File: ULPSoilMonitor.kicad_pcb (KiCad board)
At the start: 2 copper layers, 27.1 x 76.2 mm, 62 parts, among them J1 Conn_01x03_Male, J2 Conn_01x03_Male, J3 Conn_01x03_Male, J4 Conn_01x03_Male, J5 Conn_01x03_Male, J6 Conn_01x03_Male, J7 USB_B_Micro, J8 BME280_(GYBMEP), Q1 BC807, Q2 MMDT3904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

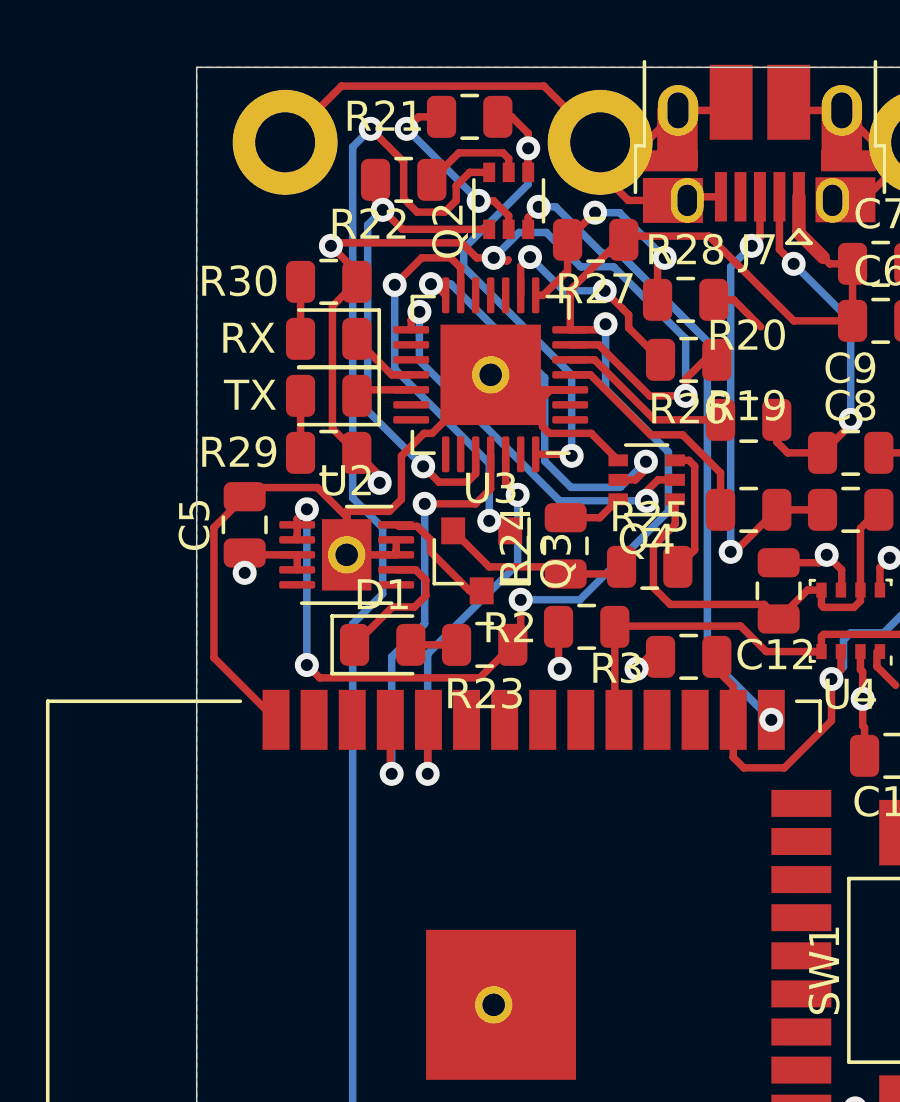
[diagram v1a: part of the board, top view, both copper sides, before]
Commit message: Layout jumpers on PCB
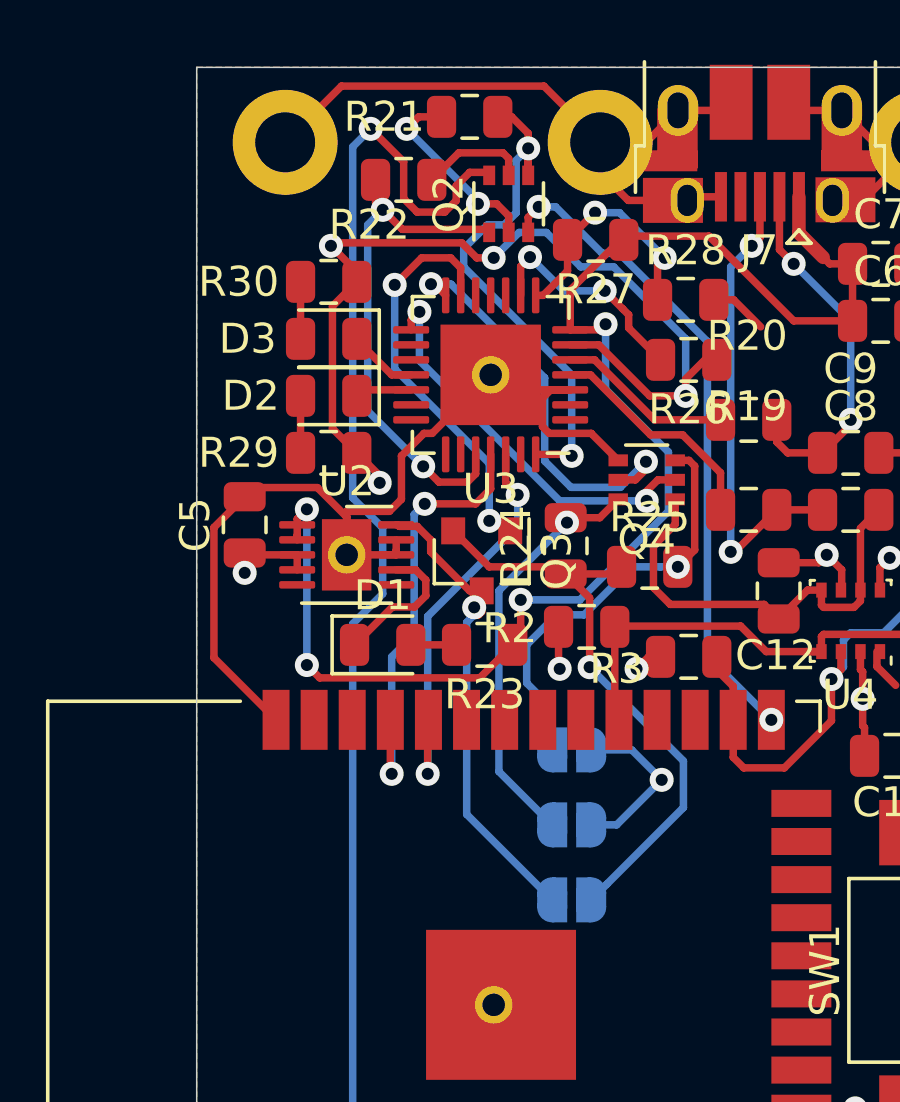
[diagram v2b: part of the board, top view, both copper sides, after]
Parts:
- added JP1: Charg_enable, Jumper:SolderJumper-2_P1.3mm_Open_RoundedPad1.0x1.5mm, B.Cu at (51.0, 56.0)
- added JP2: Charge_500mA, Jumper:SolderJumper-2_P1.3mm_Open_RoundedPad1.0x1.5mm, B.Cu at (51.0, 51.0)
- added JP3: Charge_300mA, Jumper:SolderJumper-2_P1.3mm_Open_RoundedPad1.0x1.5mm, B.Cu at (51.0, 53.5)
- moved Q2 0.10 mm to (48.9, 32.8)
- renumbered TX to D2, RX to D3
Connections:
- J7 pad 4: (no net) -> Net-(J7-Pad4)
- U1 pad 12: (no net) -> Net-(U1-Pad12)
- U1 pad 13: (no net) -> Net-(U1-Pad13)
- U1 pad 14: (no net) -> Net-(U1-Pad14)
- U1 pad 16: (no net) -> Net-(U1-Pad16)
- U1 pad 17: (no net) -> Net-(U1-Pad17)
- U1 pad 18: (no net) -> Net-(U1-Pad18)
- U1 pad 19: (no net) -> Net-(U1-Pad19)
- U1 pad 20: (no net) -> Net-(U1-Pad20)
- U1 pad 21: (no net) -> Net-(U1-Pad21)
- U1 pad 22: (no net) -> Net-(U1-Pad22)
- U1 pad 23: (no net) -> Net-(U1-Pad23)
- U1 pad 24: (no net) -> Net-(U1-Pad24)
- U1 pad 27: (no net) -> Net-(U1-Pad27)
- U1 pad 28: (no net) -> Net-(U1-Pad28)
- U1 pad 30: (no net) -> Net-(U1-Pad30)
- U1 pad 31: (no net) -> Net-(U1-Pad31)
- U1 pad 32: (no net) -> Net-(U1-Pad32)
- U1 pad 33: (no net) -> Net-(U1-Pad33)
- U1 pad 36: (no net) -> Net-(U1-Pad36)
- U1 pad 37: (no net) -> Net-(U1-Pad37)
- U2 pad : (no net) -> -BATT
- U2 pad 5: (no net) -> Net-(U2-Pad5)
- U2 pad 6: (no net) -> Net-(U2-Pad6)
- U3 pad : (no net) -> -BATT
- U3 pad 1: (no net) -> /USBtoSerial/~DCD
- U3 pad 10: (no net) -> Net-(U3-Pad10)
- U3 pad 11: (no net) -> /USBtoSerial/~SUSPENDb
- U3 pad 12: (no net) -> /USBtoSerial/SUSPEND
- U3 pad 16: (no net) -> /USBtoSerial/~WAKEUP_GPIO3
- U3 pad 17: (no net) -> /USBtoSerial/RS485_GPIO2
- U3 pad 2: (no net) -> /USBtoSerial/~RI
- U3 pad 20: (no net) -> /USBtoSerial/GPIO6
- U3 pad 21: (no net) -> /USBtoSerial/GPIO5
- U3 pad 22: (no net) -> /USBtoSerial/GPIO4
- U3 pad 23: (no net) -> /USBtoSerial/~CTS
- U3 pad 27: (no net) -> /USBtoSerial/~DSR
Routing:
- net Net-(JP1-Pad2): track 6.36 -> 20.1 mm, vias 0 -> 1
- net PROG: track 3.99 -> 15.8 mm, vias 0 -> 1
- net Net-(JP3-Pad1): track 2.00 -> 13.8 mm, vias 0 -> 1
- net Net-(JP2-Pad1): track 4.32 -> 14.3 mm, vias 0 -> 1
- net -BATT: track 102.2 -> 107.9 mm, vias 0 -> 1

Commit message: Layout
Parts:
- removed C6: 4.7μF, Capacitor_SMD:C_0805_2012Metric
- removed C7: 100nF, Capacitor_SMD:C_0805_2012Metric
- removed C8, C9: 47pF, Capacitor_SMD:C_0805_2012Metric
- removed D2: TX, LED_SMD:LED_0805_2012Metric
- removed D3: RX, LED_SMD:LED_0805_2012Metric
- removed Q2, Q4: MMDT3904, Package_TO_SOT_SMD:SOT-363_SC-70-6
- removed Q3: BC817, Package_TO_SOT_SMD:SOT-23
- removed R19, R20: 27R, Resistor_SMD:R_0805_2012Metric
- removed R21, R22: 10k, Resistor_SMD:R_0805_2012Metric
- removed R26: 1k, Resistor_SMD:R_0805_2012Metric
- removed R27: 22k1, Resistor_SMD:R_0805_2012Metric
- removed R28: 47k5, Resistor_SMD:R_0805_2012Metric
- removed R29, R30: R, Resistor_SMD:R_0805_2012Metric
- removed U3: CP2102N-A01-GQFN28, Package_DFN_QFN:QFN-28-1EP_5x5mm_P0.5mm_EP3.35x3.35mm
- added G***: LOGO, 0 - GIE Design Logos:GIE Design - no LLC (3mm x 2mm), F.Cu at (46.2, 30.2)
- added J9: USB_C_Receptacle_PowerOnly, 0 - GIE Connectors, Terminal Blocks:TYPE-C-31-M-17.kicad_mod, F.Cu at (57.3, 29.3)
- added R31: 5.1k 10%, Resistor_SMD:R_0805_2012Metric, F.Cu at (58.0, 37.0)
- added R32: 5.1k 10%, Resistor_SMD:R_0805_2012Metric, F.Cu at (56.0, 37.0)
- J7: value USB_B_Micro -> Conn_ESP_PROG_1.27mm_TagConnect; footprint Connector_USB:USB_Micro-B_Amphenol_10103594-0001LF_Horizontal -> Connector:Tag-Connect_TC2030-IDC-NL_2x03_P1.27mm_Vertical
- JP1: value Charg_enable -> Charge_enable; footprint Jumper:SolderJumper-2_P1.3mm_Open_RoundedPad1.0x1.5mm -> Jumper:SolderJumper-2_P1.3mm_Bridged_RoundedPad1.0x1.5mm
- JP2: footprint Jumper:SolderJumper-2_P1.3mm_Open_RoundedPad1.0x1.5mm -> Jumper:SolderJumper-2_P1.3mm_Bridged_RoundedPad1.0x1.5mm
- moved JP3 21.5 mm to (41.2, 34.4)
- moved JP1 19.1 mm to (41.2, 39.5), turned to 180 degrees
- moved JP2 17.1 mm to (41.2, 37.0)
- moved R25 14.9 mm to (41.0, 37.0)
- moved R24 13.4 mm to (41.0, 35.0), turned to 180 degrees
- moved J7 13.1 mm to (47.0, 39.0), turned to 90 degrees
- moved C5 1.00 mm to (40.1, 42.5)
- moved R3 0.10 mm to (54.9, 47.8)
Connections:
- J7 pad 1: VBUS -> EN
- J7 pad 2: Net-(C9-Pad1) -> +BATT
- J7 pad 3: Net-(C8-Pad1) -> ESPTX
- J7 pad 4: Net-(J7-Pad4) -> -BATT
- J7 pad 5: -BATT -> ESPRX
- J7 pad 6: -BATT -> IO0
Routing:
- net /USBtoSerial/VDD: track 31.5 -> 0.00 mm, vias 4 -> 0
- net DTR: track 17.5 -> 0.00 mm, vias 2 -> 0
- net RTS: track 17.2 -> 0.00 mm, vias 2 -> 0
- net Net-(C8-Pad1): track 16.2 -> 0.00 mm, vias 2 -> 0
- net EN: track 68.5 -> 52.7 mm
- net CHR1: track 13.9 -> 0.00 mm, vias 2 -> 0
- net Net-(JP1-Pad2): track 20.1 -> 6.29 mm
- net CHREN: track 13.6 -> 0.00 mm, vias 2 -> 0
- net CHR0: track 13.3 -> 0.00 mm, vias 2 -> 0
- net Net-(JP3-Pad1): track 13.8 -> 0.86 mm
- net Net-(C9-Pad1): track 12.4 -> 0.00 mm, vias 2 -> 0
- net VBUS: track 48.3 -> 36.8 mm
- net -BATT: track 107.9 -> 96.6 mm, vias 1 -> 0
- net PROG: track 15.8 -> 5.32 mm
- net Net-(JP2-Pad1): track 14.3 -> 4.34 mm
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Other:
- net class Default: clearance 0.2 -> 0.1778
- rule trace_clearance: 0.2 -> 0.1778

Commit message: Edit silkscreen
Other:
- board text added: "Flobs ULPSoilMonitor v2.3 2021-03-24 (Modified by ZGustafson)"
- board text removed: "Flobs ULPSoilMonitor v2.2 2020-07-05"
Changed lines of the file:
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@@
     (tags resistor)
     (attr smd)
-    (fp_text reference R32 (at 0 -1.65 90) (layer F.SilkS)
+    (fp_text reference R32 (at 3.2 0 90) (layer F.SilkS)
       (effects (font (size 1 1) (thickness 0.15)))
     )
@@
     (tags resistor)
     (attr smd)
-    (fp_text reference R31 (at 0 -1.65 90) (layer F.SilkS)
+    (fp_text reference R31 (at 3.2 0 90) (layer F.SilkS)
       (effects (font (size 1 1) (thickness 0.15)))
     )
@@
     (tags resistor)
     (attr smd)
-    (fp_text reference R23 (at 0 -1.65) (layer F.SilkS)
+    (fp_text reference R23 (at 0 1.6) (layer F.SilkS)
       (effects (font (size 1 1) (thickness 0.15)))
     )
@@
     (tags diode)
     (attr smd)
-    (fp_text reference D1 (at 0 -1.65) (layer F.SilkS)
+    (fp_text reference D1 (at -2.3 -0.1 90) (layer F.SilkS)
       (effects (font (size 1 1) (thickness 0.15)))
     )
@@
     (tags capacitor)
     (attr smd)
-    (fp_text reference C5 (at 0 -1.65 90) (layer F.SilkS)
+    (fp_text reference C5 (at 2.8 0 90) (layer F.SilkS)
       (effects (font (size 1 1) (thickness 0.15)))
     )
@@
       (effects (font (size 1 1) (thickness 0.15)))
     )
-    (fp_text value RESET (at 0 3 90) (layer F.SilkS)
+    (fp_text value RESET (at 0 2.65 90) (layer F.SilkS)
       (effects (font (size 1 1) (thickness 0.15)))
     )
@@
     (tags resistor)
     (attr smd)
-    (fp_text reference R17 (at 1.55 1.4 270) (layer F.SilkS)
+    (fp_text reference R17 (at 0 1.9 270) (layer F.SilkS)
       (effects (font (size 1 1) (thickness 0.15)))
     )
@@
     (tags resistor)
     (attr smd)
-    (fp_text reference R3 (at 2.4 -0.4) (layer F.SilkS)
+    (fp_text reference R3 (at 0 1.5) (layer F.SilkS)
       (effects (font (size 1 1) (thickness 0.15)))
     )
@@
     (descr "Through hole straight pin header, 1x04, 2.54mm pitch, single row")
     (tags "Through hole pin header THT 1x04 2.54mm single row")
-    (fp_text reference J8 (at -1.15 -2.45) (layer F.SilkS)
+    (fp_text reference J8 (at 0 -2.1) (layer F.SilkS)
       (effects (font (size 1 1) (thickness 0.15)))
     )
@@
     (tags resistor)
     (attr smd)
-    (fp_text reference R2 (at 2.5625 -0.05) (layer F.SilkS)
+    (fp_text reference R2 (at 0 1.6) (layer F.SilkS)
       (effects (font (size 1 1) (thickness 0.15)))
     )
@@
     )
   )
-  (gr_text "Flobs ULPSoilMonitor v2.2\n2020-07-05" (at 63 85.8 90) (layer F.SilkS)
-    (effects (font (size 1 1) (thickness 0.25)))
+  (gr_text "Flobs ULPSoilMonitor v2.3\n2021-03-24 (Modified by ZGustafson)" (at 63 99.7 90) (layer F.SilkS)
+    (effects (font (size 1 1) (thickness 0.25)) (justify left))
   )
   (gr_line (start 65.6 28.25) (end 38.5 28.25) (layer Edge.Cuts) (width 0.05))
